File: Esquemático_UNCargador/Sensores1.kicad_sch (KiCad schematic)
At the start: 22 parts

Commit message: Pinout sensores
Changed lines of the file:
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@@
   (junction (at 136.271 93.218) (diameter 0) (color 0 0 0 0)
   )
+  (junction (at 107.95 109.474) (diameter 0) (color 0 0 0 0)
+  )
+  (junction (at 114.173 109.474) (diameter 0) (color 0 0 0 0)
+  )
+  (junction (at 58.801 126.492) (diameter 0) (color 0 0 0 0)
+  )
   (junction (at 130.937 33.782) (diameter 0) (color 0 0 0 0)
   )
-  (junction (at 107.95 109.474) (diameter 0) (color 0 0 0 0)
-  )
-  (junction (at 114.173 109.474) (diameter 0) (color 0 0 0 0)
-  )
-  (junction (at 58.801 126.492) (diameter 0) (color 0 0 0 0)
-  )
   (junction (at 78.105 87.63) (diameter 0) (color 0 0 0 0)
   )
@@
     (stroke (width 0) (type default))
   )
-  (wire (pts (xy 130.937 33.782) (xy 130.937 33.528))
-    (stroke (width 0) (type default))
-  )
   (wire (pts (xy 78.105 112.014) (xy 81.788 112.014))
     (stroke (width 0) (type default))
@@
     (stroke (width 0) (type default))
   )
+  (wire (pts (xy 130.937 33.782) (xy 134.747 33.782))
+    (stroke (width 0) (type default))
+  )
   (wire (pts (xy 106.045 109.474) (xy 107.95 109.474))
     (stroke (width 0) (type default))
@@
     (stroke (width 0) (type default))
   )
-  (wire (pts (xy 130.937 33.782) (xy 134.747 33.782))
+  (wire (pts (xy 180.086 106.934) (xy 180.086 107.061))
+    (stroke (width 0) (type default))
+  )
+  (wire (pts (xy 125.857 33.782) (xy 130.937 33.782))
     (stroke (width 0) (type default))
   )
@@
     (stroke (width 0) (type default))
   )
-  (wire (pts (xy 125.857 33.782) (xy 130.937 33.782))
-    (stroke (width 0) (type default))
-  )
   (wire (pts (xy 114.173 109.474) (xy 125.095 109.474))
     (stroke (width 0) (type default))
@@
     (stroke (width 0) (type default))
   )
-  (wire (pts (xy 171.831 106.934) (xy 177.927 106.934))
-    (stroke (width 0) (type default))
-  )
-  (wire (pts (xy 130.937 35.052) (xy 130.937 33.782))
+  (wire (pts (xy 171.831 106.934) (xy 180.086 106.934))
+    (stroke (width 0) (type default))
+  )
+  (wire (pts (xy 130.937 33.782) (xy 130.937 35.052))
     (stroke (width 0) (type default))
   )
@@
     (effects (font (size 1.27 1.27)) (justify left bottom))
   )
-  (global_label "RX_01" (shape bidirectional) (at 77.47 40.64 0) (fields_autoplaced)
-    (effects (font (size 1.27 1.27)) (justify left))
-    (property "Intersheetrefs" "${INTERSHEET_REFS}" (at 87.3532 40.64 0)
-      (effects (font (size 1.27 1.27)) (justify left) hide)
-    )
-  )
-  (global_label "TX_01" (shape bidirectional) (at 92.71 34.29 0) (fields_autoplaced)
-    (effects (font (size 1.27 1.27)) (justify left))
-    (property "Intersheetrefs" "${INTERSHEET_REFS}" (at 102.2908 34.29 0)
-      (effects (font (size 1.27 1.27)) (justify left) hide)
-    )
-  )
-  (global_label "NTC_Analog" (shape input) (at 134.747 33.782 0) (fields_autoplaced)
-    (effects (font (size 1.27 1.27)) (justify left))
-    (property "Intersheetrefs" "${INTERSHEET_REFS}" (at 148.5383 33.782 0)
-      (effects (font (size 1.27 1.27)) (justify left) hide)
-    )
-  )
-  (global_label "GFCI_TEST" (shape input) (at 64.135 77.724 0) (fields_autoplaced)
-    (effects (font (size 1.27 1.27)) (justify left))
-    (property "Intersheetrefs" "${INTERSHEET_REFS}" (at 76.5355 77.724 0)
-      (effects (font (size 1.27 1.27)) (justify left) hide)
-    )
-  )
-  (global_label "FALLA" (shape input) (at 177.927 106.934 0) (fields_autoplaced)
-    (effects (font (size 1.27 1.27)) (justify left))
-    (property "Intersheetrefs" "${INTERSHEET_REFS}" (at 186.1548 106.934 0)
-      (effects (font (size 1.27 1.27)) (justify left) hide)
-    )
+  (hierarchical_label "TX_01" (shape input) (at 92.71 34.29 0) (fields_autoplaced)
+    (effects (font (size 1.27 1.27)) (justify left))
+  )
+  (hierarchical_label "NTC_Analog" (shape input) (at 134.747 33.782 0) (fields_autoplaced)
+    (effects (font (size 1.27 1.27)) (justify left))
+  )
+  (hierarchical_label "FALLA" (shape input) (at 180.086 107.061 0) (fields_autoplaced)
+    (effects (font (size 1.27 1.27)) (justify left))
+  )
+  (hierarchical_label "GFCI_TEST" (shape input) (at 64.135 77.724 0) (fields_autoplaced)
+    (effects (font (size 1.27 1.27)) (justify left))
+  )
+  (hierarchical_label "RX_01" (shape input) (at 77.47 40.64 0) (fields_autoplaced)
+    (effects (font (size 1.27 1.27)) (justify left))
   )
   (symbol (lib_id "Device:R") (at 67.945 106.934 270) (unit 1)

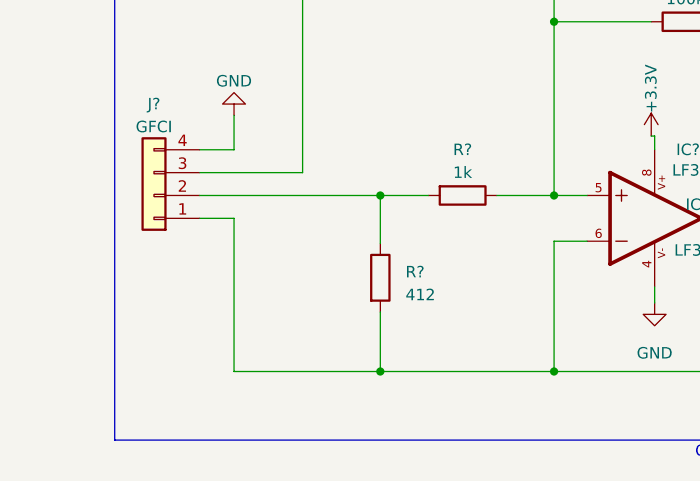
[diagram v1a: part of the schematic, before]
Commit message: zener sensores con huellas
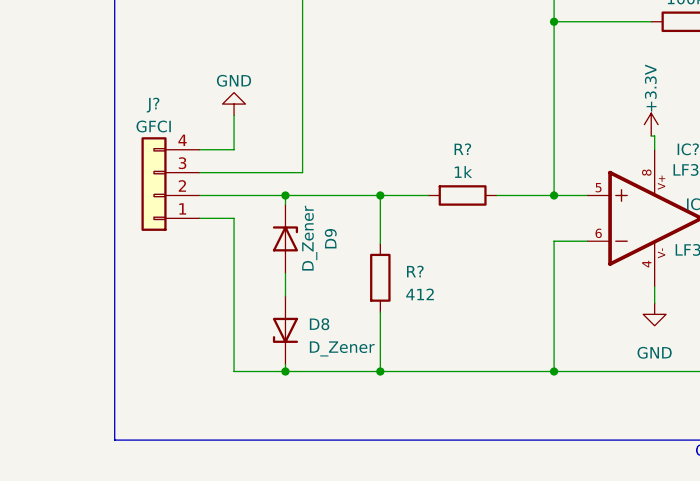
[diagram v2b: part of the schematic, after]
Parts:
- added D8, D9: D_Zener, DO214AC:DO-214AC, symbol Device:D_Zener
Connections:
- net GND: now also D8.1 (K)
- net at J?.2 (Pin_2), R?.1, R?.2: now also D9.1 (K)
- new net: D8.2 (A), D9.2 (A)
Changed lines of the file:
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@@
   (junction (at 78.105 126.492) (diameter 0) (color 0 0 0 0)
   )
+  (junction (at 48.26 106.934) (diameter 0) (color 0 0 0 0)
+  )
   (junction (at 107.95 87.63) (diameter 0) (color 0 0 0 0)
   )
@@
   (junction (at 136.271 93.218) (diameter 0) (color 0 0 0 0)
   )
+  (junction (at 48.26 126.492) (diameter 0) (color 0 0 0 0)
+  )
   (junction (at 107.95 109.474) (diameter 0) (color 0 0 0 0)
   )
@@
     (stroke (width 0) (type default))
   )
+  (wire (pts (xy 48.26 115.57) (xy 48.26 118.11))
+    (stroke (width 0) (type default))
+  )
   (wire (pts (xy 78.105 112.014) (xy 78.105 126.492))
     (stroke (width 0) (type default))
@@
     (stroke (width 0) (type default))
   )
-  (wire (pts (xy 42.545 126.492) (xy 58.801 126.492))
+  (wire (pts (xy 42.545 126.492) (xy 48.26 126.492))
     (stroke (width 0) (type default))
   )
@@
     (stroke (width 0) (type default))
   )
-  (wire (pts (xy 38.735 106.934) (xy 58.801 106.934))
+  (wire (pts (xy 38.735 106.934) (xy 48.26 106.934))
     (stroke (width 0) (type default))
   )
@@
     (stroke (width 0) (type default))
   )
+  (wire (pts (xy 48.26 126.492) (xy 58.801 126.492))
+    (stroke (width 0) (type default))
+  )
   (wire (pts (xy 78.105 126.492) (xy 104.775 126.492))
     (stroke (width 0) (type default))
@@
     (stroke (width 0) (type default))
   )
+  (wire (pts (xy 48.26 106.934) (xy 58.801 106.934))
+    (stroke (width 0) (type default))
+  )
   (wire (pts (xy 58.801 106.934) (xy 64.135 106.934))
     (stroke (width 0) (type default))
@@
     (stroke (width 0) (type default))
   )
+  (wire (pts (xy 48.26 106.934) (xy 48.26 107.95))
+    (stroke (width 0) (type default))
+  )
   (wire (pts (xy 58.801 119.888) (xy 58.801 126.492))
+    (stroke (width 0) (type default))
+  )
+  (wire (pts (xy 48.26 125.73) (xy 48.26 126.492))
     (stroke (width 0) (type default))
   )
@@
     )
   )
+  (symbol (lib_id "Device:D_Zener") (at 48.26 111.76 270) (unit 1)
+    (in_bom yes) (on_board yes) (dnp no)
+    (property "Reference" "D9" (at 53.34 111.76 0)
+      (effects (font (size 1.27 1.27)))
+    )
+    (property "Value" "D_Zener" (at 50.8 111.76 0)
+      (effects (font (size 1.27 1.27)))
+    )
+    (property "Footprint" "DO214AC:DO-214AC" (at 48.26 111.76 0)
+      (effects (font (size 1.27 1.27)) hide)
+    )
+    (property "Datasheet" "~" (at 48.26 111.76 0)
+      (effects (font (size 1.27 1.27)) hide)
+    )
+    (pin "1")
+    (pin "2")
+    (instances
+      (project "CircuitoPotencia"
+        (path "/f64e4c48-29c2-4644-b6e3-d55b9152fc29/bcc2cbe9-78c8-42aa-91d0-1fe918a34d54"
+          (reference "D9") (unit 1)
+        )
+      )
+    )
+  )
   (symbol (lib_id "power:GND") (at 130.937 43.942 0) (unit 1)
     (in_bom yes) (on_board yes) (dnp no) (fields_autoplaced)
@@
         )
       )
+    )
+  )
+  (symbol (lib_id "Device:D_Zener") (at 48.26 121.92 90) (unit 1)
+    (in_bom yes) (on_board yes) (dnp no) (fields_autoplaced)
+    (property "Reference" "D8" (at 50.8 121.285 90)
+      (effects (font (size 1.27 1.27)) (justify right))
+    )
+    (property "Value" "D_Zener" (at 50.8 123.825 90)
+      (effects (font (size 1.27 1.27)) (justify right))
+    )
+    (property "Footprint" "DO214AC:DO-214AC" (at 48.26 121.92 0)
+      (effects (font (size 1.27 1.27)) hide)
+    )
+    (property "Datasheet" "~" (at 48.26 121.92 0)
+      (effects (font (size 1.27 1.27)) hide)
+    )
+    (pin "1")
+    (pin "2")
+    (instances
+      (project "CircuitoPotencia"
+        (path "/f64e4c48-29c2-4644-b6e3-d55b9152fc29/bcc2cbe9-78c8-42aa-91d0-1fe918a34d54"
+          (reference "D8") (unit 1)
+        )
+      )

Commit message: Actualización Sensores
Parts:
- D8, D9: value D_Zener -> SMAZ5V1
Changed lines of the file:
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@@
       (effects (font (size 1.27 1.27)))
     )
-    (property "Value" "D_Zener" (at 50.8 111.76 0)
+    (property "Value" "SMAZ5V1" (at 50.8 111.76 0)
       (effects (font (size 1.27 1.27)))
     )
@@
       (effects (font (size 1.27 1.27)) (justify right))
     )
-    (property "Value" "D_Zener" (at 50.8 123.825 90)
+    (property "Value" "SMAZ5V1" (at 50.8 123.825 90)
       (effects (font (size 1.27 1.27)) (justify right))
     )

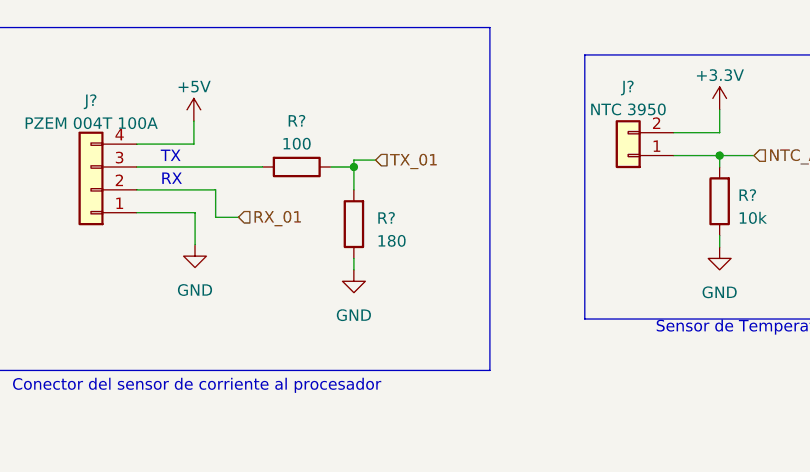
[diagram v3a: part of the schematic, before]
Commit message: Modificación de la huella del microcontrolador
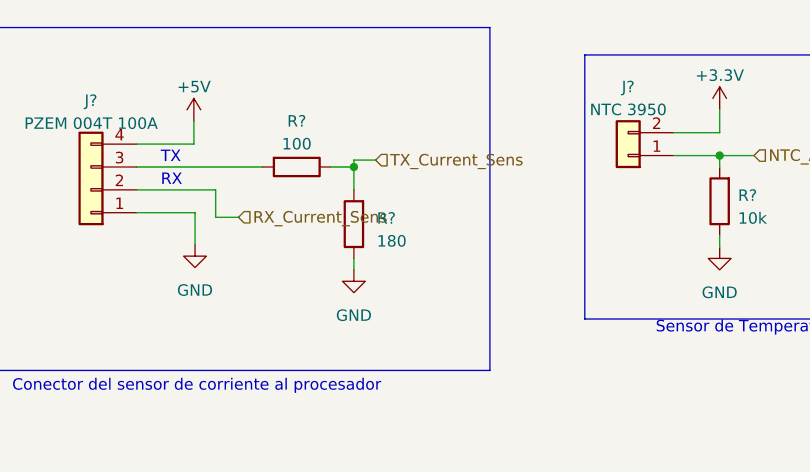
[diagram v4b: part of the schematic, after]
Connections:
- net RX_01 renamed RX_Current_Sens
- net TX_01 renamed TX_Current_Sens
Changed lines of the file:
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@@
     (effects (font (size 1.27 1.27)) (justify left bottom))
   )
-  (hierarchical_label "TX_01" (shape input) (at 92.71 34.29 0) (fields_autoplaced)
+  (hierarchical_label "TX_Current_Sens" (shape input) (at 92.71 34.29 0) (fields_autoplaced)
     (effects (font (size 1.27 1.27)) (justify left))
   )
@@
     (effects (font (size 1.27 1.27)) (justify left))
   )
-  (hierarchical_label "RX_01" (shape input) (at 77.47 40.64 0) (fields_autoplaced)
+  (hierarchical_label "RX_Current_Sens" (shape input) (at 77.47 40.64 0) (fields_autoplaced)
     (effects (font (size 1.27 1.27)) (justify left))
   )

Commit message: Modificación relays
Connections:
- net RX_Current_Sens renamed RX_Pzem
- net TX_Current_Sens renamed TX_Pzem
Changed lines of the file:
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@@
     (effects (font (size 1.27 1.27)) (justify left bottom))
   )
-  (hierarchical_label "TX_Current_Sens" (shape input) (at 92.71 34.29 0) (fields_autoplaced)
+  (hierarchical_label "TX_Pzem" (shape input) (at 92.71 34.29 0) (fields_autoplaced)
     (effects (font (size 1.27 1.27)) (justify left))
   )
@@
     (effects (font (size 1.27 1.27)) (justify left))
   )
-  (hierarchical_label "RX_Current_Sens" (shape input) (at 77.47 40.64 0) (fields_autoplaced)
+  (hierarchical_label "RX_Pzem" (shape input) (at 77.47 40.64 0) (fields_autoplaced)
     (effects (font (size 1.27 1.27)) (justify left))
   )

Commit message: Cambios de recomendaciones profesor
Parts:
- removed J?: ALIMENTACION, Connector_JST:JST_EH_B2B-EH-A_1x02_P2.50mm_Vertical, symbol Connector_Generic:Conn_01x02
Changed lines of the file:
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@@
-    (stroke (width 0) (type default))
-  )
-  (wire (pts (xy 36.068 28.575) (xy 36.068 27.94))
     (stroke (width 0) (type default))
   )
@@
     (stroke (width 0) (type default))
   )
-  (wire (pts (xy 31.75 25.4) (xy 35.941 25.4))
-    (stroke (width 0) (type default))
-  )
   (wire (pts (xy 130.937 33.782) (xy 134.747 33.782))
     (stroke (width 0) (type default))
@@
     (stroke (width 0) (type default))
   )
-  (wire (pts (xy 36.068 27.94) (xy 31.75 27.94))
-    (stroke (width 0) (type default))
-  )
   (wire (pts (xy 180.086 106.934) (xy 180.086 107.061))
     (stroke (width 0) (type default))
@@
   )
   (wire (pts (xy 74.93 40.64) (xy 77.47 40.64))
-    (stroke (width 0) (type default))
-  )
-  (wire (pts (xy 35.941 25.4) (xy 35.941 25.019))
     (stroke (width 0) (type default))
   )
@@
     )
   )
-  (symbol (lib_id "power:VCC") (at 35.941 25.019 0) (unit 1)
-    (in_bom yes) (on_board yes) (dnp no) (fields_autoplaced)
-    (property "Reference" "#PWR?" (at 35.941 28.829 0)
-      (effects (font (size 1.27 1.27)) hide)
-    )
-    (property "Value" "VCC" (at 35.941 21.209 0)
-      (effects (font (size 1.27 1.27)))
-    )
-    (property "Footprint" "" (at 35.941 25.019 0)
-      (effects (font (size 1.27 1.27)) hide)
-    )
-    (property "Datasheet" "" (at 35.941 25.019 0)
-      (effects (font (size 1.27 1.27)) hide)
-    )
-    (pin "1")
-    (instances
-      (project "Sensores"
-        (path "/c520d7c0-a0b4-4308-b262-cba91039e873"
-          (reference "#PWR?") (unit 1)
-        )
-      )
-      (project "CircuitoPotencia"
-        (path "/f64e4c48-29c2-4644-b6e3-d55b9152fc29/bcc2cbe9-78c8-42aa-91d0-1fe918a34d54"
-          (reference "#PWR018") (unit 1)
-        )
-      )
-    )
-  )
   (symbol (lib_id "Device:R") (at 128.397 93.218 90) (unit 1)
     (in_bom yes) (on_board yes) (dnp no) (fields_autoplaced)
@@
         (path "/f64e4c48-29c2-4644-b6e3-d55b9152fc29/bcc2cbe9-78c8-42aa-91d0-1fe918a34d54"
           (reference "D5") (unit 1)
-        )
-      )
-    )
-  )
-  (symbol (lib_id "power:GND") (at 36.068 28.575 0) (unit 1)
-    (in_bom yes) (on_board yes) (dnp no) (fields_autoplaced)
-    (property "Reference" "#PWR?" (at 36.068 34.925 0)
-      (effects (font (size 1.27 1.27)) hide)
-    )
-    (property "Value" "GND" (at 36.068 33.655 0)
-      (effects (font (size 1.27 1.27)))
-    )
-    (property "Footprint" "" (at 36.068 28.575 0)
-      (effects (font (size 1.27 1.27)) hide)
-    )
-    (property "Datasheet" "" (at 36.068 28.575 0)
-      (effects (font (size 1.27 1.27)) hide)
-    )
-    (pin "1")
-    (instances
-      (project "Sensores"
-        (path "/c520d7c0-a0b4-4308-b262-cba91039e873"
-          (reference "#PWR?") (unit 1)
-        )
-      )
-      (project "CircuitoPotencia"
-        (path "/f64e4c48-29c2-4644-b6e3-d55b9152fc29/bcc2cbe9-78c8-42aa-91d0-1fe918a34d54"
-          (reference "#PWR019") (unit 1)
         )
       )
@@
         )
       )
-    )
-  )
-  (symbol (lib_id "Connector_Generic:Conn_01x02") (at 26.67 27.94 180) (unit 1)
-    (in_bom yes) (on_board yes) (dnp no) (fields_autoplaced)
-    (property "Reference" "J?" (at 26.67 19.812 0)
-      (effects (font (size 1.27 1.27)))
-    )
-    (property "Value" "ALIMENTACION" (at 26.67 22.352 0)
-      (effects (font (size 1.27 1.27)))
-    )
-    (property "Footprint" "Connector_JST:JST_EH_B2B-EH-A_1x02_P2.50mm_Vertical" (at 26.67 27.94 0)
-      (effects (font (size 1.27 1.27)) hide)
-    )
-    (property "Datasheet" "~" (at 26.67 27.94 0)
-      (effects (font (size 1.27 1.27)) hide)
-    )
-    (pin "1")
-    (pin "2")
-    (instances
-      (project "Sensores"
-        (path "/c520d7c0-a0b4-4308-b262-cba91039e873"
-          (reference "J?") (unit 1)
-        )
-      )
-      (project "CircuitoPotencia"
-        (path "/f64e4c48-29c2-4644-b6e3-d55b9152fc29/bcc2cbe9-78c8-42aa-91d0-1fe918a34d54"
-          (reference "J3") (unit 1)
-        )
-      )

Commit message: version inicial layout PCB
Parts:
- D8, D9: footprint DO214AC:DO-214AC -> Esquemático_UNCargador:DO-214AC
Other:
- moved on the sheet: C?, D8, D9, D?, IC?A, IC?B, IC?C, R?
